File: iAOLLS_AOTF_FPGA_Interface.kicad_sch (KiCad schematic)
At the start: 0 parts

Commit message: power schematic
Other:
- added sheet AOTF Output (AOTF_Output.kicad_sch)
- added sheet Analog Switch (Analog_Switch.kicad_sch)
- added sheet FPGA Input (FPGA_Input.kicad_sch)
- added sheet Power (Power.kicad_sch)
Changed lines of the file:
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@@
 	(generator_version "10.0")
 	(paper "A4")
+	(sheet
+		(at 139.7 46.99)
+		(size 60.96 41.91)
+		(exclude_from_sim no)
+		(in_bom yes)
+		(on_board yes)
+		(dnp no)
+		(fields_autoplaced yes)
+		(stroke
+			(width 0.1524)
+			(type solid)
+		)
+		(fill
+			(color 0 0 0 0)
+		)
+		(property "Sheetname" "FPGA Input"
+			(at 139.7 46.2784 0)
+			(show_name no)
+			(do_not_autoplace no)
+			(effects
+				(font
+					(size 1.27 1.27)
+				)
+				(justify left bottom)
+			)
+		)
+		(property "Sheetfile" "FPGA_Input.kicad_sch"
+			(at 139.7 89.4846 0)
+			(show_name no)
+			(do_not_autoplace no)
+			(effects
+				(font
+					(size 1.27 1.27)
+				)
+				(justify left top)
+			)
+		)
+		(instances
+			(project "iAOLLS_AOTF_FPGA_Interface"
+				(path "/194710d2-c7e3-4b3e-93c6-2b6cf88164b3"
+					(page "3")
+				)
+			)
+		)
+	)
+	(sheet
+		(at 66.04 110.49)
+		(size 60.96 41.91)
+		(exclude_from_sim no)
+		(in_bom yes)
+		(on_board yes)
+		(dnp no)
+		(fields_autoplaced yes)
+		(stroke
+			(width 0.1524)
+			(type solid)
+		)
+		(fill
+			(color 0 0 0 0)
+		)
+		(property "Sheetname" "Analog Switch"
+			(at 66.04 109.7784 0)
+			(show_name no)
+			(do_not_autoplace no)
+			(effects
+				(font
+					(size 1.27 1.27)
+				)
+				(justify left bottom)
+			)
+		)
+		(property "Sheetfile" "Analog_Switch.kicad_sch"
+			(at 66.04 152.9846 0)
+			(show_name no)
+			(do_not_autoplace no)
+			(effects
+				(font
+					(size 1.27 1.27)
+				)
+				(justify left top)
+			)
+		)
+		(instances
+			(project "iAOLLS_AOTF_FPGA_Interface"
+				(path "/194710d2-c7e3-4b3e-93c6-2b6cf88164b3"
+					(page "4")
+				)
+			)
+		)
+	)
+	(sheet
+		(at 139.7 110.49)
+		(size 60.96 41.91)
+		(exclude_from_sim no)
+		(in_bom yes)
+		(on_board yes)
+		(dnp no)
+		(fields_autoplaced yes)
+		(stroke
+			(width 0.1524)
+			(type solid)
+		)
+		(fill
+			(color 0 0 0 0)
+		)
+		(property "Sheetname" "AOTF Output"
+			(at 139.7 109.7784 0)
+			(show_name no)
+			(do_not_autoplace no)
+			(effects
+				(font
+					(size 1.27 1.27)
+				)
+				(justify left bottom)
+			)
+		)
+		(property "Sheetfile" "AOTF_Output.kicad_sch"
+			(at 139.7 152.9846 0)
+			(show_name no)
+			(do_not_autoplace no)
+			(effects
+				(font
+					(size 1.27 1.27)
+				)
+				(justify left top)
+			)
+		)
+		(instances
+			(project "iAOLLS_AOTF_FPGA_Interface"
+				(path "/194710d2-c7e3-4b3e-93c6-2b6cf88164b3"
+					(page "5")
+				)
+			)
+		)
+	)
+	(sheet
+		(at 66.04 46.99)
+		(size 60.96 41.91)
+		(exclude_from_sim no)
+		(in_bom yes)
+		(on_board yes)
+		(dnp no)
+		(fields_autoplaced yes)
+		(stroke
+			(width 0.1524)
+			(type solid)
+		)
+		(fill
+			(color 0 0 0 0)
+		)
+		(property "Sheetname" "Power"
+			(at 66.04 46.2784 0)
+			(show_name no)
+			(do_not_autoplace no)
+			(effects
+				(font
+					(size 1.27 1.27)
+				)
+				(justify left bottom)
+			)
+		)
+		(property "Sheetfile" "Power.kicad_sch"
+			(at 66.04 89.4846 0)
+			(show_name no)
+			(do_not_autoplace no)
+			(effects
+				(font
+					(size 1.27 1.27)
+				)
+				(justify left top)
+			)
+		)
+		(instances
+			(project "iAOLLS_AOTF_FPGA_Interface"
+				(path "/194710d2-c7e3-4b3e-93c6-2b6cf88164b3"
+					(page "2")
+				)
+			)
+		)
+	)
 	(sheet_instances
 		(path "/"

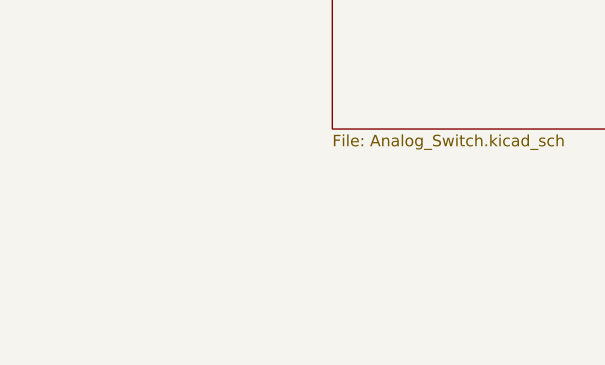
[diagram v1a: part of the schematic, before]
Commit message: fix drc errors and add mounting holes
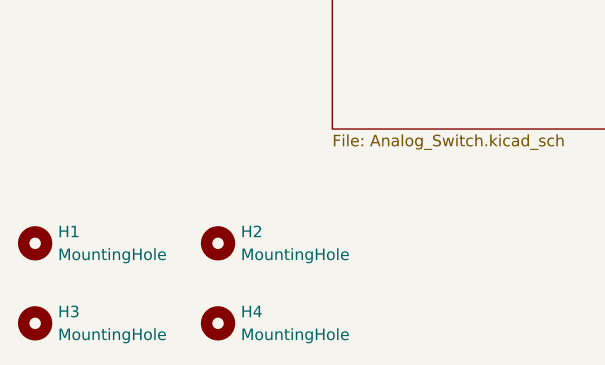
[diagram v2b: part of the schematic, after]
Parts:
- added H1, H2, H3, H4: MountingHole, MountingHole:MountingHole_3.2mm_M3_Pad_Via, symbol Mechanical:MountingHole
